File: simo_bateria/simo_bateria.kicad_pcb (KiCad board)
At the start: 2 copper layers, 4 parts, among them J1 conector, U1 simo_bateria, U2 cargador_bateria

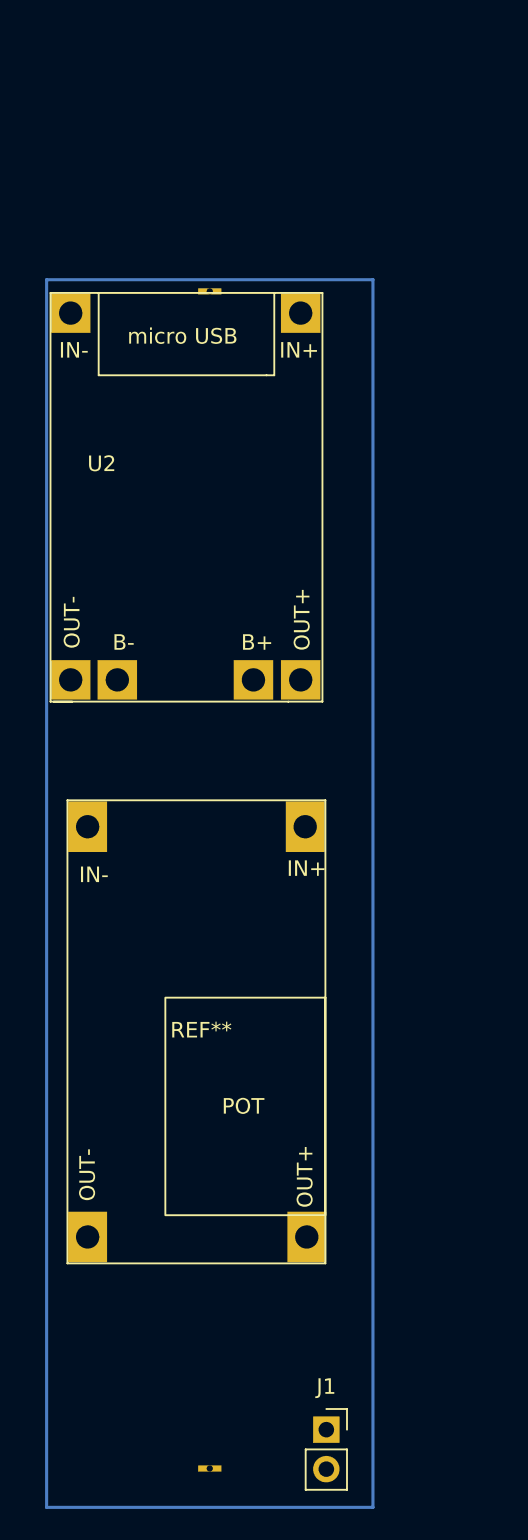
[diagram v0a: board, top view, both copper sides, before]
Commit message: se completaron todos los modelos 3d y se verifico las footprint
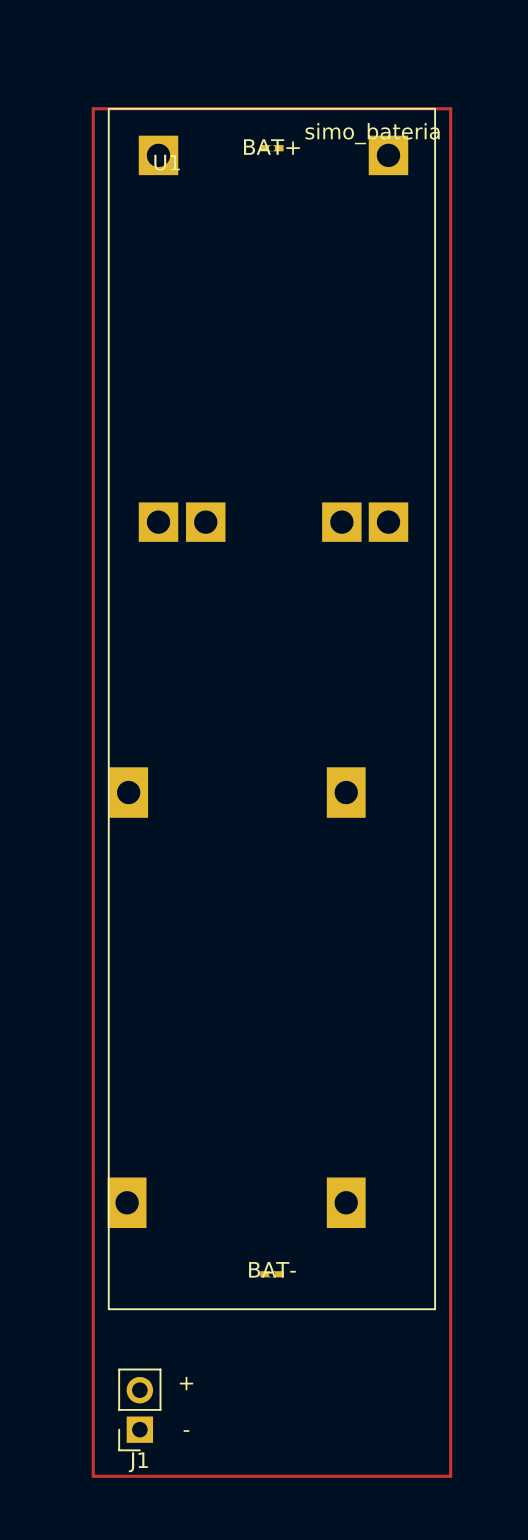
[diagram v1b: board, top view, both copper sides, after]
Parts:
- removed REF**: conversor_dc_dc, simo_bateria:conversor_dc_dc
- added U3: conversor_dc, simo_bateria:conversor_dc_dc, B.Cu at (135.3, 74.0)
- J1: value conector -> conector salida
- U1: moved to F.Cu
- U2: moved to B.Cu
- moved U2 22.8 mm to (138.0, 33.0), turned to 180 degrees
- moved J1 12.0 mm to (122.0, 115.0), turned to 180 degrees
- moved U1 11.7 mm to (130.5, 30.0), turned to 0 degrees
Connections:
- U2 pad 3: Net-(J1-Pad1) -> Net-(U2-Pad3)
- U2 pad 5: Net-(J1-Pad2) -> Net-(U2-Pad5)
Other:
- board text added: "+"
- board text added: "-"

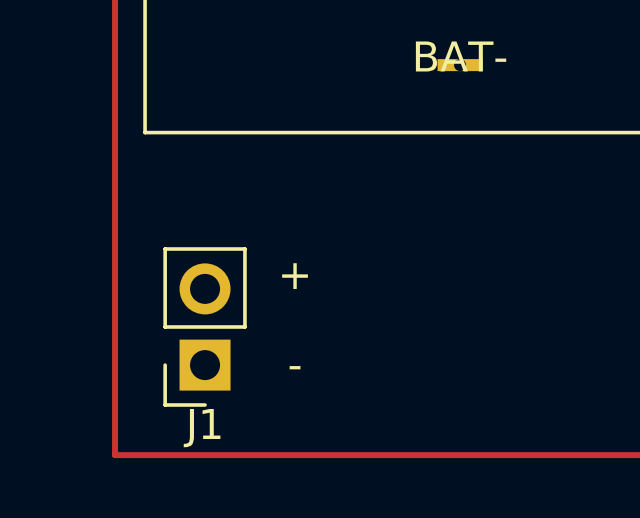
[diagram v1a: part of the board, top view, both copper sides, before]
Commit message: se hizo mas compacta pcb shield
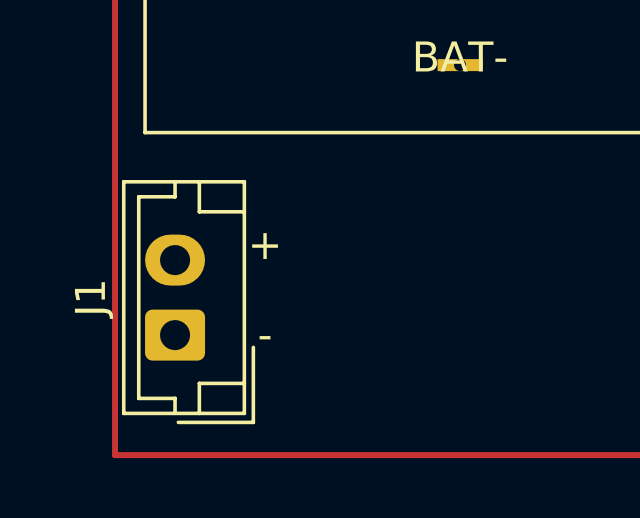
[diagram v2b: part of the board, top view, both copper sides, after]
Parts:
- J1: footprint Connector_PinSocket_2.54mm:PinSocket_1x02_P2.54mm_Vertical -> Connector_JST:JST_EH_B2B-EH-A_1x02_P2.50mm_Vertical
- moved J1 1.41 mm to (121.0, 114.0), turned to 90 degrees
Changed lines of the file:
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@@
   (net 7 "unconnected-(U2-Pad4)")
   (net 8 "Net-(U2-Pad5)")
-  (footprint "Connector_PinSocket_2.54mm:PinSocket_1x02_P2.54mm_Vertical" (layer "F.Cu")
-    (at 122 115 180)
-    (descr "Through hole straight socket strip, 1x02, 2.54mm pitch, single row (from Kicad 4.0.7), script generated")
-    (tags "Through hole socket strip THT 1x02 2.54mm single row")
-    (property "Sheetfile" "simo_bateria.kicad_sch")
-    (property "Sheetname" "")
-    (attr through_hole)
-    (fp_text reference "J1" (at 0 -2) (layer "F.SilkS")
-      (effects (font (size 1 1) (thickness 0.15)))
-    )
-    (fp_text value "conector salida" (at -4 5.31) (layer "F.Fab")
-      (effects (font (size 1 1) (thickness 0.15)))
-    )
-    (fp_text user "${REFERENCE}" (at 0 1.27 90) (layer "F.Fab")
-      (effects (font (size 1 1) (thickness 0.15)))
-    )
-    (fp_line (start -1.33 1.27) (end 1.33 1.27) (layer "F.SilkS") (width 0.12))
-    (fp_line (start 1.33 -1.33) (end 1.33 0) (layer "F.SilkS") (width 0.12))
-    (fp_line (start 0 -1.33) (end 1.33 -1.33) (layer "F.SilkS") (width 0.12))
-    (fp_line (start 1.33 1.27) (end 1.33 3.87) (layer "F.SilkS") (width 0.12))
-    (fp_line (start -1.33 3.87) (end 1.33 3.87) (layer "F.SilkS") (width 0.12))
-    (fp_line (start -1.33 1.27) (end -1.33 3.87) (layer "F.SilkS") (width 0.12))
-    (fp_line (start 1.75 -1.8) (end 1.75 4.3) (layer "F.CrtYd") (width 0.05))
-    (fp_line (start -1.8 -1.8) (end 1.75 -1.8) (layer "F.CrtYd") (width 0.05))
-    (fp_line (start -1.8 4.3) (end -1.8 -1.8) (layer "F.CrtYd") (width 0.05))
-    (fp_line (start 1.75 4.3) (end -1.8 4.3) (layer "F.CrtYd") (width 0.05))
-    (fp_line (start 1.27 3.81) (end -1.27 3.81) (layer "F.Fab") (width 0.1))
-    (fp_line (start 1.27 -0.635) (end 1.27 3.81) (layer "F.Fab") (width 0.1))
-    (fp_line (start 0.635 -1.27) (end 1.27 -0.635) (layer "F.Fab") (width 0.1))
-    (fp_line (start -1.27 3.81) (end -1.27 -1.27) (layer "F.Fab") (width 0.1))
-    (fp_line (start -1.27 -1.27) (end 0.635 -1.27) (layer "F.Fab") (width 0.1))
-    (pad "1" thru_hole rect (at 0 0 180) (size 1.7 1.7) (drill 1) (layers *.Cu *.Mask)
-      (net 1 "Net-(J1-Pad1)") (pinfunction "Pin_1") (pintype "passive"))
-    (pad "2" thru_hole oval (at 0 2.54 180) (size 1.7 1.7) (drill 1) (layers *.Cu *.Mask)
-      (net 2 "Net-(J1-Pad2)") (pinfunction "Pin_2") (pintype "passive"))
-    (model "${KICAD6_3DMODEL_DIR}/Connector_PinSocket_2.54mm.3dshapes/PinSocket_1x02_P2.54mm_Vertical.wrl"
-      (offset (xyz 0 0 0))
-      (scale (xyz 1 1 1))
-      (rotate (xyz 0 0 0))
-    )
-  )
   (footprint "simo_bateria:bateria" (layer "F.Cu")
     (at 130.5 30)
@@
       (scale (xyz 1 1 1))
       (rotate (xyz 0 0 90))
+    )
+  )
+  (footprint "Connector_JST:JST_EH_B2B-EH-A_1x02_P2.50mm_Vertical" (layer "F.Cu")
+    (at 121 114 90)
+    (descr "JST EH series connector, B2B-EH-A (http://www.jst-mfg.com/product/pdf/eng/eEH.pdf), generated with kicad-footprint-generator")
+    (tags "connector JST EH vertical")
+    (property "Sheetfile" "simo_bateria.kicad_sch")
+    (property "Sheetname" "")
+    (attr through_hole)
+    (fp_text reference "J1" (at 1.25 -2.8 90) (layer "F.SilkS")
+      (effects (font (size 1 1) (thickness 0.15)))
+    )
+    (fp_text value "conector salida" (at -2 9 180) (layer "F.Fab")
+      (effects (font (size 1 1) (thickness 0.15)))
+    )
+    (fp_text user "${REFERENCE}" (at 1.25 1.5 90) (layer "F.Fab")
+      (effects (font (size 1 1) (thickness 0.15)))
+    )
+    (fp_line (start -1.61 0.81) (end -1.61 2.31) (layer "F.SilkS") (width 0.12))
+    (fp_line (start -2.61 -1.71) (end -2.61 2.31) (layer "F.SilkS") (width 0.12))
+    (fp_line (start 4.61 -1.21) (end 4.61 0) (layer "F.SilkS") (width 0.12))
+    (fp_line (start 4.11 0.81) (end 4.11 2.31) (layer "F.SilkS") (width 0.12))
+    (fp_line (start -2.61 0) (end -2.11 0) (layer "F.SilkS") (width 0.12))
+    (fp_line (start -2.11 -1.21) (end 4.61 -1.21) (layer "F.SilkS") (width 0.12))
+    (fp_line (start -2.11 0) (end -2.11 -1.21) (layer "F.SilkS") (width 0.12))
+    (fp_line (start -2.91 0.11) (end -2.91 2.61) (layer "F.SilkS") (width 0.12))
+    (fp_line (start -2.61 2.31) (end 5.11 2.31) (layer "F.SilkS") (width 0.12))
+    (fp_line (start 5.11 -1.71) (end -2.61 -1.71) (layer "F.SilkS") (width 0.12))
+    (fp_line (start -2.61 0.81) (end -1.61 0.81) (layer "F.SilkS") (width 0.12))
+    (fp_line (start -2.91 2.61) (end -0.41 2.61) (layer "F.SilkS") (width 0.12))
+    (fp_line (start 5.11 2.31) (end 5.11 -1.71) (layer "F.SilkS") (width 0.12))
+    (fp_line (start 4.61 0) (end 5.11 0) (layer "F.SilkS") (width 0.12))
+    (fp_line (start 5.11 0.81) (end 4.11 0.81) (layer "F.SilkS") (width 0.12))
+    (fp_line (start -3 2.7) (end 5.5 2.7) (layer "F.CrtYd") (width 0.05))
+    (fp_line (start -3 -2.1) (end -3 2.7) (layer "F.CrtYd") (width 0.05))
+    (fp_line (start 5.5 -2.1) (end -3 -2.1) (layer "F.CrtYd") (width 0.05))
+    (fp_line (start 5.5 2.7) (end 5.5 -2.1) (layer "F.CrtYd") (width 0.05))
+    (fp_line (start -2.5 -1.6) (end -2.5 2.2) (layer "F.Fab") (width 0.1))
+    (fp_line (start -2.91 2.61) (end -0.41 2.61) (layer "F.Fab") (width 0.1))
+    (fp_line (start -2.5 2.2) (end 5 2.2) (layer "F.Fab") (width 0.1))
+    (fp_line (start 5 2.2) (end 5 -1.6) (layer "F.Fab") (width 0.1))
+    (fp_line (start -2.91 0.11) (end -2.91 2.61) (layer "F.Fab") (width 0.1))
+    (fp_line (start 5 -1.6) (end -2.5 -1.6) (layer "F.Fab") (width 0.1))
+    (pad "1" thru_hole roundrect (at 0 0 90) (size 1.7 2) (drill 1) (layers *.Cu *.Mask) (roundrect_rratio 0.147059)
+      (net 1 "Net-(J1-Pad1)") (pinfunction "Pin_1") (pintype "passive"))
+    (pad "2" thru_hole oval (at 2.5 0 90) (size 1.7 2) (drill 1) (layers *.Cu *.Mask)
+      (net 2 "Net-(J1-Pad2)") (pinfunction "Pin_2") (pintype "passive"))
+    (model "${KICAD6_3DMODEL_DIR}/Connector_JST.3dshapes/JST_EH_B2B-EH-A_1x02_P2.50mm_Vertical.wrl"
+      (offset (xyz 0 0 0))
+      (scale (xyz 1 1 1))
+      (rotate (xyz 0 0 0))
     )
   )
@@
   )
   (gr_rect (start 119 30) (end 142 118) (layer "F.Cu") (width 0.2) (fill none))
-  (gr_text "-\n" (at 125 115) (layer "F.SilkS")
+  (gr_text "-\n" (at 124 114) (layer "F.SilkS")
     (effects (font (size 1 1) (thickness 0.15)))
   )
-  (gr_text "+" (at 125 112) (layer "F.SilkS")
+  (gr_text "+" (at 124 111) (layer "F.SilkS")
     (effects (font (size 1 1) (thickness 0.15)))
   )

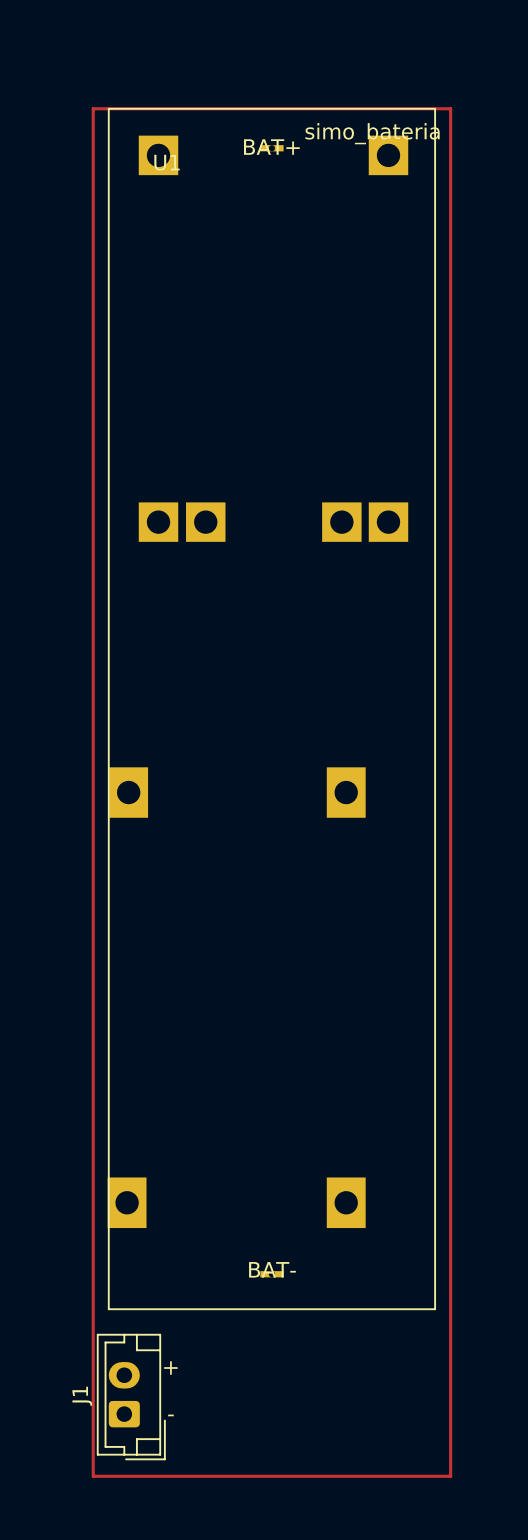
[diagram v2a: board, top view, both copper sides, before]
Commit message: se agrego conector de bateria a ambas placas
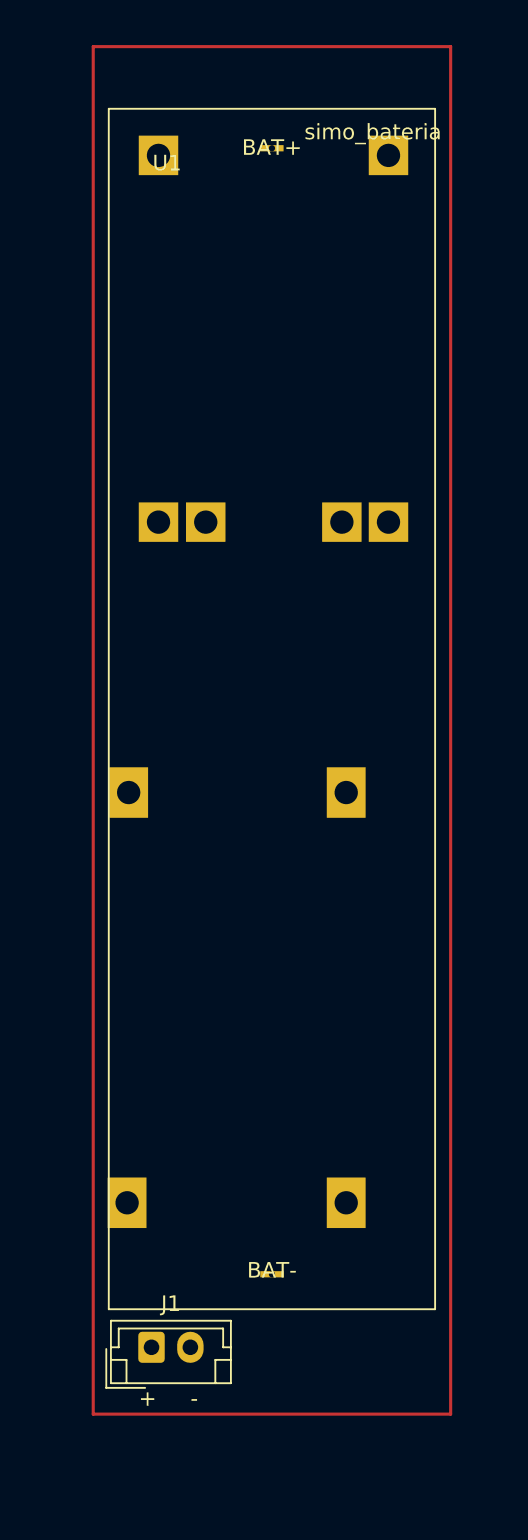
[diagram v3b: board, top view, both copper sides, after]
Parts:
- moved J1 4.64 mm to (122.8, 109.7), turned to 0 degrees
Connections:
- J1 pad 1: Net-(J1-Pad1) -> Net-(U3-Pad4)
- J1 pad 2: Net-(J1-Pad2) -> Net-(U3-Pad2)
- U3 pad 2: Net-(J1-Pad1) -> Net-(U3-Pad2)
- U3 pad 4: Net-(J1-Pad2) -> Net-(U3-Pad4)
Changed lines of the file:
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@@
   )
   (net 0 "")
-  (net 1 "Net-(J1-Pad1)")
-  (net 2 "Net-(J1-Pad2)")
+  (net 1 "Net-(U3-Pad4)")
+  (net 2 "Net-(U3-Pad2)")
   (net 3 "Net-(U1-Pad1)")
   (net 4 "Net-(U1-Pad2)")
@@
   )
   (footprint "Connector_JST:JST_EH_B2B-EH-A_1x02_P2.50mm_Vertical" (layer "F.Cu")
-    (at 121 114 90)
+    (at 122.75 109.7)
     (descr "JST EH series connector, B2B-EH-A (http://www.jst-mfg.com/product/pdf/eng/eEH.pdf), generated with kicad-footprint-generator")
     (tags "connector JST EH vertical")
@@
     (property "Sheetname" "")
     (attr through_hole)
-    (fp_text reference "J1" (at 1.25 -2.8 90) (layer "F.SilkS")
-      (effects (font (size 1 1) (thickness 0.15)))
-    )
-    (fp_text value "conector salida" (at -2 9 180) (layer "F.Fab")
-      (effects (font (size 1 1) (thickness 0.15)))
-    )
-    (fp_text user "${REFERENCE}" (at 1.25 1.5 90) (layer "F.Fab")
+    (fp_text reference "J1" (at 1.25 -2.8) (layer "F.SilkS")
+      (effects (font (size 1 1) (thickness 0.15)))
+    )
+    (fp_text value "conector salida" (at 12.25 -1.2 180) (layer "F.Fab")
+      (effects (font (size 1 1) (thickness 0.15)))
+    )
+    (fp_text user "${REFERENCE}" (at 1.25 1.5) (layer "F.Fab")
       (effects (font (size 1 1) (thickness 0.15)))
     )
@@
     (fp_line (start -2.91 0.11) (end -2.91 2.61) (layer "F.Fab") (width 0.1))
     (fp_line (start 5 -1.6) (end -2.5 -1.6) (layer "F.Fab") (width 0.1))
-    (pad "1" thru_hole roundrect (at 0 0 90) (size 1.7 2) (drill 1) (layers *.Cu *.Mask) (roundrect_rratio 0.147059)
-      (net 1 "Net-(J1-Pad1)") (pinfunction "Pin_1") (pintype "passive"))
-    (pad "2" thru_hole oval (at 2.5 0 90) (size 1.7 2) (drill 1) (layers *.Cu *.Mask)
-      (net 2 "Net-(J1-Pad2)") (pinfunction "Pin_2") (pintype "passive"))
-    (model "${KICAD6_3DMODEL_DIR}/Connector_JST.3dshapes/JST_EH_B2B-EH-A_1x02_P2.50mm_Vertical.wrl"
+    (pad "1" thru_hole roundrect (at 0 0) (size 1.7 2) (drill 1) (layers *.Cu *.Mask) (roundrect_rratio 0.147059)
+      (net 1 "Net-(U3-Pad4)") (pinfunction "Pin_1") (pintype "passive"))
+    (pad "2" thru_hole oval (at 2.5 0) (size 1.7 2) (drill 1) (layers *.Cu *.Mask)
+      (net 2 "Net-(U3-Pad2)") (pinfunction "Pin_2") (pintype "passive"))
+    (model "/home/gvelardez/simo_pcb/proyecto_definitivo/simo_pcb/simo_pcb/simo/otros/JST-B2B-EH-A.STEP"
       (offset (xyz 0 0 0))
       (scale (xyz 1 1 1))
-      (rotate (xyz 0 0 0))
+      (rotate (xyz -90 0 0))
     )
   )
@@
       (net 6 "Net-(U2-Pad3)") (pinfunction "VIN-") (pintype "input"))
     (pad "2" thru_hole rect (at 0 -26.4 180) (size 2.5 3.25) (drill 1.5) (layers *.Cu *.Mask)
-      (net 1 "Net-(J1-Pad1)") (pinfunction "VOUT-") (pintype "power_out"))
+      (net 2 "Net-(U3-Pad2)") (pinfunction "VOUT-") (pintype "power_out"))
     (pad "3" thru_hole rect (at 14 0 180) (size 2.5 3.25) (drill 1.5) (layers *.Cu *.Mask)
       (net 8 "Net-(U2-Pad5)") (pinfunction "VIN+") (pintype "power_in"))
     (pad "4" thru_hole rect (at 14.1 -26.4 180) (size 2.5 3.25) (drill 1.5) (layers *.Cu *.Mask)
-      (net 2 "Net-(J1-Pad2)") (pinfunction "VOUT+") (pintype "power_in"))
+      (net 1 "Net-(U3-Pad4)") (pinfunction "VOUT+") (pintype "power_in"))
     (model "/home/gvelardez/simo_pcb/proyecto_definitivo/simo_pcb/simo_pcb/simo/otros/conversor/MT3608 Converter.STEP"
       (offset (xyz 6.5 -13.5 0))
@@
     )
   )
-  (gr_rect (start 119 30) (end 142 118) (layer "F.Cu") (width 0.2) (fill none))
-  (gr_text "-\n" (at 124 114) (layer "F.SilkS")
+  (gr_rect (start 119 26) (end 142 114) (layer "F.Cu") (width 0.2) (fill none))
+  (gr_text "-\n" (at 125.5 113) (layer "F.SilkS")
     (effects (font (size 1 1) (thickness 0.15)))
   )
-  (gr_text "+" (at 124 111) (layer "F.SilkS")
+  (gr_text "+" (at 122.5 113) (layer "F.SilkS")
     (effects (font (size 1 1) (thickness 0.15)))
   )

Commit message: se guardaron modelos 3d de ambas placas en formato step
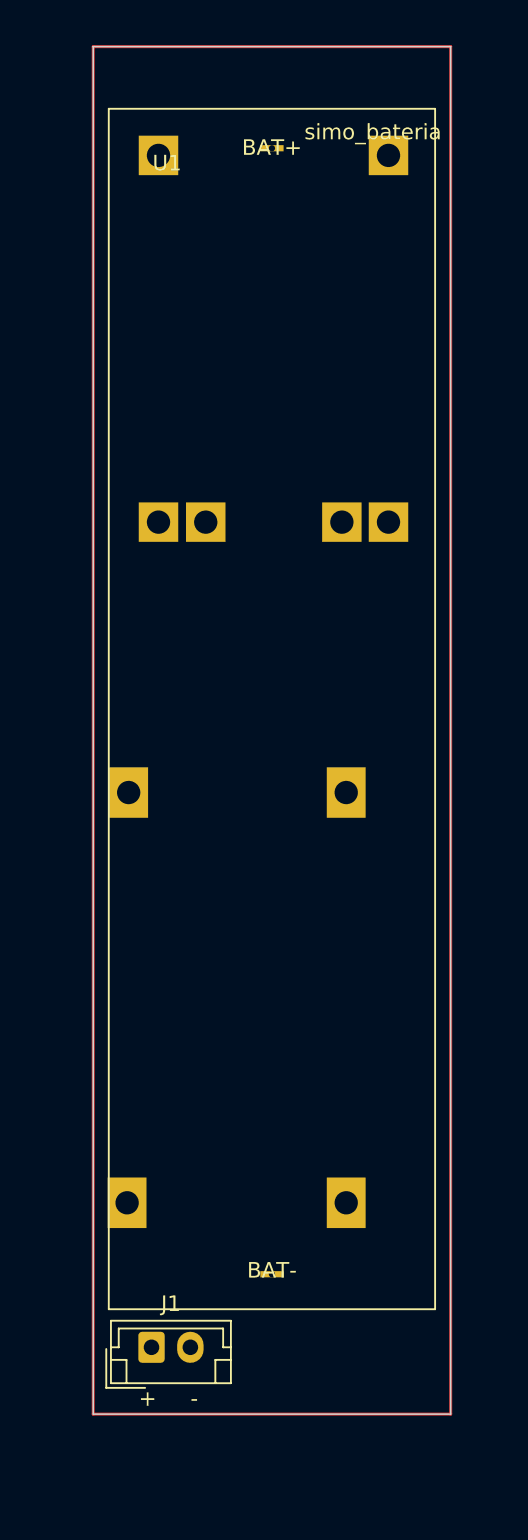
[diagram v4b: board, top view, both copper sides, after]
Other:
- board outline added: 23 x 88 mm
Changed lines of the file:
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@@
   )
   (gr_rect (start 119 26) (end 142 114) (layer "F.Cu") (width 0.2) (fill none))
+  (gr_rect (start 119 26) (end 142 114) (layer "Edge.Cuts") (width 0.1) (fill none))
   (gr_text "-\n" (at 125.5 113) (layer "F.SilkS")
     (effects (font (size 1 1) (thickness 0.15)))
